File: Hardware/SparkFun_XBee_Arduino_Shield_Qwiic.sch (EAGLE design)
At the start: 68 parts, among them J4 QWIIC_RIGHT_ANGLE, U1 FSUSB30MUX_MSOP10, U2 AP63203, U3 ESD Diode, U4 FT231XS, U5 ESD Diode, U6 TXS0108, U7 TXS0108

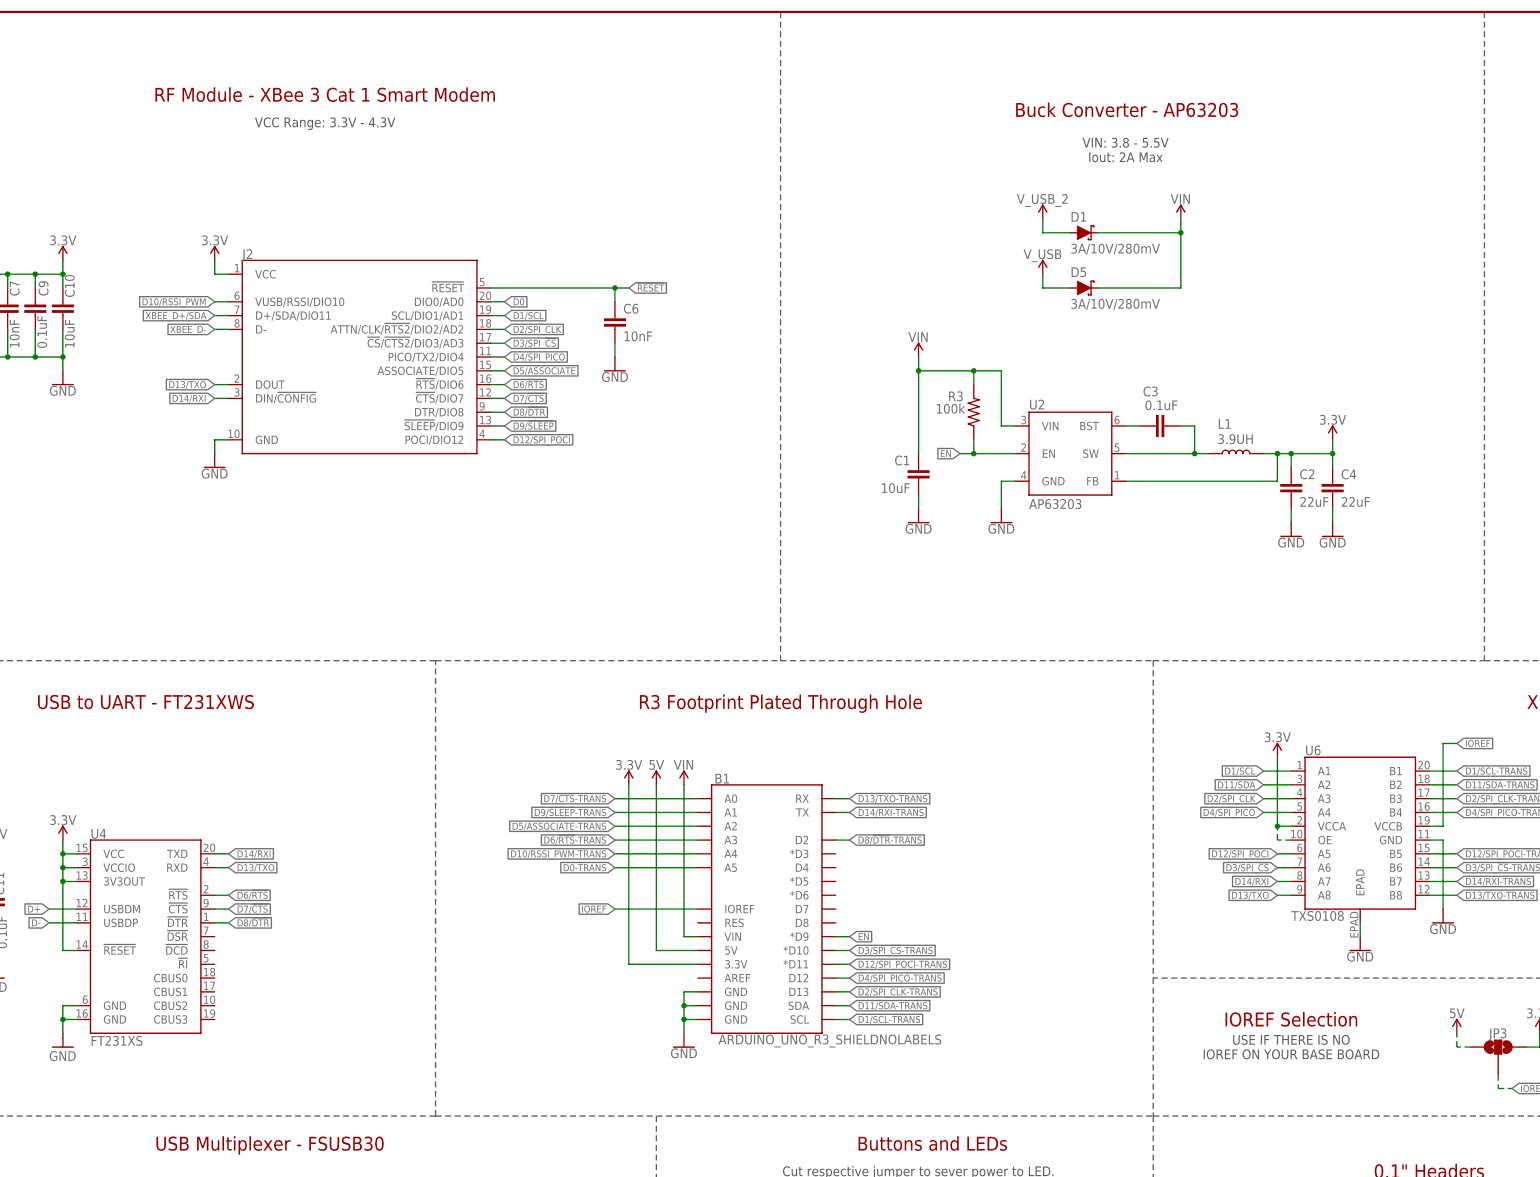
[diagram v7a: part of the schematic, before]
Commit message: Adds "1, 2, 3, 4" to layers and special ordering instructions
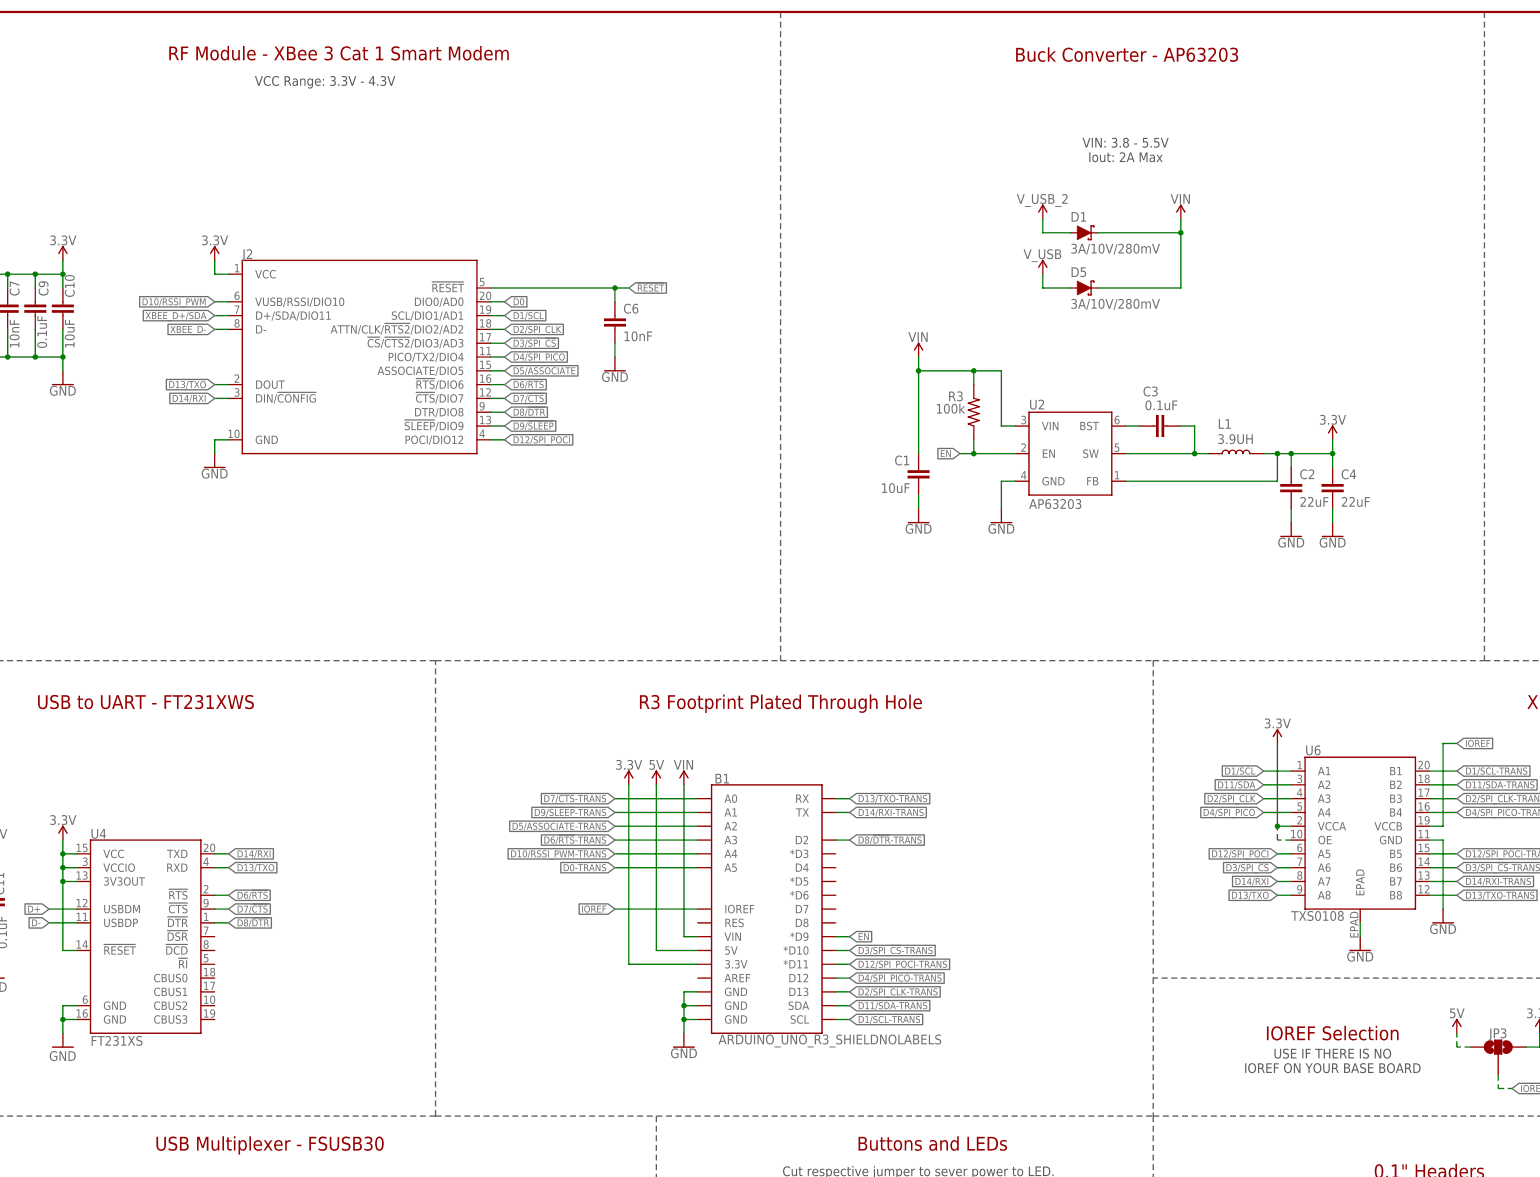
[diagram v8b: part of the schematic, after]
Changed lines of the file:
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@@
 <sheet>
 <plain>
-<text x="76.2" y="259.08" size="1.778" layer="97" font="vector" align="center">VCC Range: 3.3V - 4.3V</text>
-<text x="223.774" y="261.366" size="2.54" layer="94" font="vector" align="center">Buck Converter - AP63203</text>
+<text x="76.2" y="266.7" size="1.778" layer="97" font="vector" align="center">VCC Range: 3.3V - 4.3V</text>
+<text x="223.774" y="271.526" size="2.54" layer="94" font="vector" align="center">Buck Converter - AP63203</text>
 <text x="388.62" y="93.98" size="2.54" layer="94" font="vector" align="center">Qwiic - I2C</text>
 <text x="424.18" y="7.62" size="2.54" layer="94" font="vector" align="center">v01</text>
@@
 <text x="388.62" y="88.9" size="1.778" layer="97" font="vector" align="center">Cut I2C jumper to remove pullups.</text>
 <text x="185.42" y="66.04" size="1.778" layer="97" font="vector" align="center">Cut respective jumper to sever power to LED.</text>
-<text x="76.2" y="264.16" size="2.54" layer="94" font="vector" align="center">RF Module - XBee 3 Cat 1 Smart Modem</text>
+<text x="78.74" y="271.78" size="2.54" layer="94" font="vector" align="center">RF Module - XBee 3 Cat 1 Smart Modem</text>
 <text x="279.4" y="66.04" size="2.54" layer="94" font="vector" align="center">0.1" Headers</text>
 <text x="380.746" y="208.788" size="1.778" layer="97" font="vector">Cut SHLD/SHLD1 jumper to disconnect
@@
 <text x="327.66" y="147.32" size="1.778" layer="97" font="vector" align="center">3.3V (VCCA) -&gt; 3.3V - 5V (VCCB)</text>
 <wire x1="330.2" y1="101.6" x2="228.6" y2="101.6" width="0.2032" layer="97" style="longdash"/>
-<text x="254" y="93.98" size="2.54" layer="94" font="vector" align="center">IOREF Selection </text>
-<text x="254" y="88.9" size="1.778" layer="97" font="vector" align="center">USE IF THERE IS NO
+<text x="261.62" y="91.44" size="2.54" layer="94" font="vector" align="center">IOREF Selection </text>
+<text x="261.62" y="86.36" size="1.778" layer="97" font="vector" align="center">USE IF THERE IS NO
 IOREF ON YOUR BASE BOARD</text>
 <text x="66.04" y="71.12" size="2.54" layer="94" font="vector" align="center">USB Multiplexer - FSUSB30</text>
@@
 <attribute name="VALUE" x="281.94" y="111.506" size="1.778" layer="96" font="vector" rot="MR0" align="top-center"/>
 </instance>
-<instance part="SUPPLY21" gate="G$1" x="251.46" y="142.24" smashed="yes" rot="MR0">
-<attribute name="VALUE" x="251.46" y="145.034" size="1.778" layer="96" font="vector" rot="MR0" align="bottom-center"/>
+<instance part="SUPPLY21" gate="G$1" x="251.46" y="144.78" smashed="yes" rot="MR0">
+<attribute name="VALUE" x="251.46" y="147.574" size="1.778" layer="96" font="vector" rot="MR0" align="bottom-center"/>
 </instance>
 <instance part="GND20" gate="1" x="266.7" y="106.68" smashed="yes" rot="MR0">
@@
 <pinref part="U6" gate="G$1" pin="VCCA"/>
 <wire x1="254" y1="129.54" x2="251.46" y2="129.54" width="0.1524" layer="91"/>
-<wire x1="251.46" y1="129.54" x2="251.46" y2="142.24" width="0.1524" layer="91"/>
+<wire x1="251.46" y1="129.54" x2="251.46" y2="144.78" width="0.1524" layer="91"/>
 <pinref part="SUPPLY21" gate="G$1" pin="3.3V"/>
 <pinref part="U6" gate="G$1" pin="OE"/>
